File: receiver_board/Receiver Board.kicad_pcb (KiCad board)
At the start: 4 copper layers, 24.8 x 17.5 mm, 12 parts, among them P4 SERIAL, SW1 SW_DPST, U1 LM3671, U2 ESP-01, U3 NeoPixel, U4 SN74LVC1T45

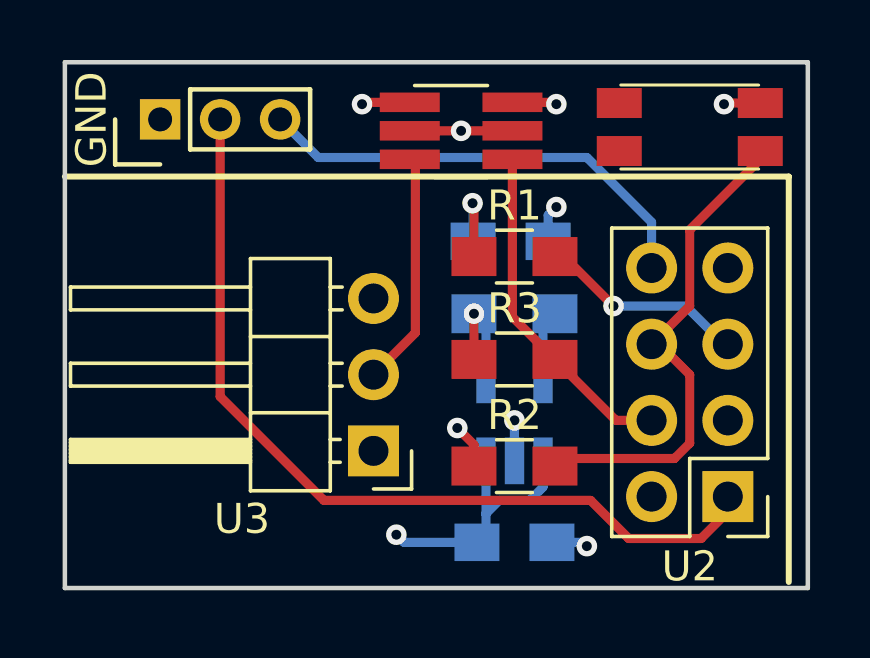
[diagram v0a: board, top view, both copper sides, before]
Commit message: Revised receiver board
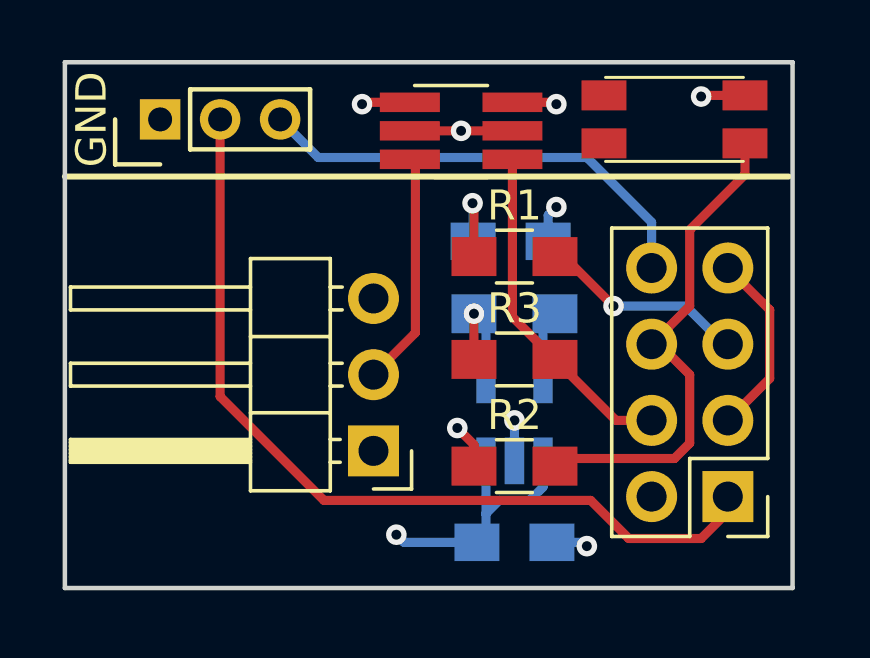
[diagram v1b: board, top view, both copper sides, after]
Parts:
- moved SW1 0.57 mm to (148.0, 132.1)
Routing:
- net VCC: track 9.96 -> 16.2 mm
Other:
- board size 24.8 x 17.5 mm -> 24.3 x 17.5 mm
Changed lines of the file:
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@@
     (links 29)
     (no_connects 0)
-    (area 124.8026 116.600409 152.475001 155.015001)
+    (area 124.8026 116.600409 152.475001 148.082001)
     (thickness 1.6)
-    (drawings 8)
-    (tracks 78)
+    (drawings 7)
+    (tracks 81)
     (zones 0)
     (modules 12)
@@
     (descr "Through hole straight pin header, 2x04, 2.54mm pitch, double rows")
     (tags "Through hole pin header THT 2x04 2.54mm double row")
-    (fp_text reference U2 (at 1.27 -2.33 180) (layer F.SilkS)
+    (fp_text reference U2 (at 1.27 -2.33 180) (layer F.SilkS) hide
       (effects (font (size 1 1) (thickness 0.15)))
     )
@@
     (descr "Through hole angled pin header, 1x03, 2.54mm pitch, 6mm pin length, single row")
     (tags "Through hole angled pin header THT 1x03 2.54mm single row")
-    (fp_text reference U3 (at 4.385 -2.27 180) (layer F.SilkS)
+    (fp_text reference U3 (at 4.385 -2.27 180) (layer F.SilkS) hide
       (effects (font (size 1 1) (thickness 0.15)))
     )
@@
   )
   (module nebrius-switch:KMR641NG (layer F.Cu)
-    (at 148.463 132.334 180)
+    (at 147.955 132.08 180)
     (fp_text reference SW1 (at 0 4 180) (layer F.SilkS) hide
       (effects (font (size 1 1) (thickness 0.15)))
@@
     )
   )
-  (gr_line (start 127.635 130.175) (end 152.4 130.175) (angle 90) (layer Edge.Cuts) (width 0.15))
-  (gr_line (start 127.635 147.701) (end 152.4 147.701) (angle 90) (layer Edge.Cuts) (width 0.15))
+  (gr_line (start 127.635 130.175) (end 151.892 130.175) (angle 90) (layer Edge.Cuts) (width 0.15))
+  (gr_line (start 127.635 147.701) (end 151.892 147.701) (angle 90) (layer Edge.Cuts) (width 0.15))
   (gr_line (start 127.635 130.175) (end 127.635 147.701) (angle 90) (layer Edge.Cuts) (width 0.15))
-  (gr_line (start 152.4 147.701) (end 152.4 130.175) (angle 90) (layer Edge.Cuts) (width 0.15))
+  (gr_line (start 151.892 147.701) (end 151.892 130.175) (angle 90) (layer Edge.Cuts) (width 0.15))
   (gr_text "Raver Lights\nReceiver 3.0\nCopyright\nBryan Hughes" (at 132.08 140.97 90) (layer B.SilkS)
     (effects (font (size 1.016 1.016) (thickness 0.1524)) (justify mirror))
@@
   )
   (gr_line (start 151.765 133.985) (end 127.635 133.985) (angle 90) (layer F.SilkS) (width 0.2))
-  (gr_line (start 151.765 147.5) (end 151.765 133.985) (angle 90) (layer F.SilkS) (width 0.2))
   (segment (start 143.571 140.763) (end 143.571 138.957) (width 0.3048) (layer B.Cu) (net 1))
   (segment (start 143.571 138.957) (end 143.971 138.557) (width 0.3048) (layer B.Cu) (net 1))
@@
   (via (at 137.541 131.572) (size 0.6858) (drill 0.3302) (layers F.Cu B.Cu) (net 2))
   (segment (start 137.602 131.511) (end 137.541 131.572) (width 0.3048) (layer F.Cu) (net 2))
+  (segment (start 150.305 131.28) (end 148.882 131.28) (width 0.3048) (layer F.Cu) (net 3))
+  (via (at 148.844 131.318) (size 0.6858) (drill 0.3302) (layers F.Cu B.Cu) (net 3))
+  (segment (start 148.882 131.28) (end 148.844 131.318) (width 0.3048) (layer F.Cu) (net 3))
   (segment (start 143.744 136.144) (end 143.744 135.275) (width 0.3048) (layer B.Cu) (net 3))
   (via (at 144.018 135.001) (size 0.6858) (drill 0.3302) (layers F.Cu B.Cu) (net 3))
@@
   (segment (start 142.621 143.463) (end 142.621 142.113) (width 0.3048) (layer B.Cu) (net 3))
   (via (at 142.621 142.113) (size 0.6858) (drill 0.3302) (layers F.Cu B.Cu) (net 3))
-  (segment (start 150.813 131.534) (end 149.644 131.534) (width 0.3048) (layer F.Cu) (net 3))
-  (via (at 149.606 131.572) (size 0.6858) (drill 0.3302) (layers F.Cu B.Cu) (net 3))
-  (segment (start 149.644 131.534) (end 149.606 131.572) (width 0.3048) (layer F.Cu) (net 3))
+  (segment (start 149.733 137.033) (end 151.13 138.43) (width 0.3048) (layer F.Cu) (net 4))
+  (segment (start 151.13 140.716) (end 149.733 142.113) (width 0.3048) (layer F.Cu) (net 4))
+  (segment (start 151.13 138.43) (end 151.13 140.716) (width 0.3048) (layer F.Cu) (net 4))
   (segment (start 141.271 143.637) (end 141.271 142.922) (width 0.3048) (layer F.Cu) (net 4))
   (via (at 140.716 142.367) (size 0.6858) (drill 0.3302) (layers F.Cu B.Cu) (net 4))
@@
   (segment (start 145.923 138.303) (end 144.272 136.652) (width 0.3048) (layer F.Cu) (net 7))
   (segment (start 144.272 136.652) (end 143.971 136.652) (width 0.3048) (layer F.Cu) (net 7))
+  (segment (start 150.305 132.88) (end 150.305 133.921) (width 0.3048) (layer F.Cu) (net 8))
+  (segment (start 148.463 138.303) (end 147.193 139.573) (width 0.3048) (layer F.Cu) (net 8))
+  (segment (start 148.463 135.763) (end 148.463 138.303) (width 0.3048) (layer F.Cu) (net 8))
+  (segment (start 150.305 133.921) (end 148.463 135.763) (width 0.3048) (layer F.Cu) (net 8))
   (segment (start 147.193 139.573) (end 147.447 139.573) (width 0.3048) (layer F.Cu) (net 8))
   (segment (start 147.447 139.573) (end 148.463 140.589) (width 0.3048) (layer F.Cu) (net 8))
@@
   (segment (start 148.463 140.589) (end 148.463 142.875) (width 0.3048) (layer F.Cu) (net 8))
   (segment (start 144.225 143.383) (end 143.971 143.637) (width 0.3048) (layer F.Cu) (net 8))
-  (segment (start 150.813 133.134) (end 150.813 133.413) (width 0.3048) (layer F.Cu) (net 8))
-  (segment (start 150.813 133.413) (end 148.463 135.763) (width 0.3048) (layer F.Cu) (net 8))
-  (segment (start 148.463 135.763) (end 148.463 138.303) (width 0.3048) (layer F.Cu) (net 8))
-  (segment (start 148.463 138.303) (end 147.193 139.573) (width 0.3048) (layer F.Cu) (net 8))
   (segment (start 142.553 133.411) (end 142.553 138.663) (width 0.3048) (layer F.Cu) (net 9))
   (segment (start 142.553 138.663) (end 143.971 140.081) (width 0.3048) (layer F.Cu) (net 9))
@@
     (polygon
       (pts
-        (xy 152.4 148.082) (xy 127.635 148.082) (xy 127.635 130.175) (xy 152.4 130.175)
+        (xy 152.4 147.701) (xy 127.635 147.701) (xy 127.635 130.175) (xy 152.4 130.175)
       )
     )
@@
     (polygon
       (pts
-        (xy 139.446 148.082) (xy 127.635 148.082) (xy 127.635 130.175) (xy 139.446 130.175)
+        (xy 139.446 147.701) (xy 127.635 147.701) (xy 127.635 130.175) (xy 139.446 130.175)
       )
     )
@@
     (polygon
       (pts
-        (xy 152.4 148.082) (xy 140.081 148.082) (xy 140.081 130.175) (xy 152.4 130.175)
+        (xy 151.892 147.701) (xy 140.081 147.701) (xy 140.081 130.175) (xy 151.892 130.175)
       )
     )

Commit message: Added copyright date
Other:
- board text added: "Raver Lights Receiver 3.0 Copyright 2018 Bryan Hughes"
- board text removed: "Raver Lights Receiver 3.0 Copyright Bryan Hughes"
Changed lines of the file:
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@@
   (gr_line (start 127.635 130.175) (end 127.635 147.701) (angle 90) (layer Edge.Cuts) (width 0.15))
   (gr_line (start 151.892 147.701) (end 151.892 130.175) (angle 90) (layer Edge.Cuts) (width 0.15))
-  (gr_text "Raver Lights\nReceiver 3.0\nCopyright\nBryan Hughes" (at 132.08 140.97 90) (layer B.SilkS)
+  (gr_text "Raver Lights\nReceiver 3.0\nCopyright 2018\nBryan Hughes" (at 132.08 140.97 90) (layer B.SilkS)
     (effects (font (size 1.016 1.016) (thickness 0.1524)) (justify mirror))
   )

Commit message: Added BOM and fuse
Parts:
- added F1: Fuse, Resistors_SMD:R_0805_HandSoldering, F.Cu at (140.0, 146.2)
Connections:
- C1 pad 1: +5V -> Net-(C1-Pad1)
- U1 pad 1: +5V -> Net-(C1-Pad1)
- U1 pad 3: +5V -> Net-(C1-Pad1)
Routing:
- net +5V: track 10.4 -> 3.09 mm
- net Net-(C1-Pad1): track 0.00 -> 6.12 mm, vias 0 -> 1
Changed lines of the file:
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@@
 (kicad_pcb (version 4) (host pcbnew 4.0.7)
   (general
-    (links 29)
+    (links 30)
     (no_connects 0)
-    (area 124.8026 116.600409 152.475001 148.082001)
+    (area 127.559999 130.099999 151.967001 147.776001)
     (thickness 1.6)
     (drawings 7)
-    (tracks 81)
+    (tracks 83)
     (zones 0)
-    (modules 12)
-    (nets 11)
+    (modules 13)
+    (nets 12)
   )
   (page A4)
@@
   (net 9 "Net-(R3-Pad2)")
   (net 10 "Net-(U3-Pad2)")
+  (net 11 "Net-(C1-Pad1)")
   (net_class Default "This is the default net class."
     (clearance 0.1524)
@@
     (add_net +5V)
     (add_net GND)
+    (add_net "Net-(C1-Pad1)")
     (add_net "Net-(L1-Pad1)")
     (add_net "Net-(P4-Pad2)")
@@
     (fp_line (start -0.5 -0.85) (end 0.5 -0.85) (layer B.SilkS) (width 0.15))
     (pad 1 smd rect (at -1.25 0) (size 1.5 1.25) (layers B.Cu B.Paste B.Mask)
-      (net 2 +5V))
+      (net 11 "Net-(C1-Pad1)"))
     (pad 2 smd rect (at 1.25 0) (size 1.5 1.25) (layers B.Cu B.Paste B.Mask)
       (net 3 GND))
@@
     (fp_line (start 2.38 -1.8) (end -2.38 -1.8) (layer B.CrtYd) (width 0.05))
     (pad 1 smd rect (at -1.35 0.95 90) (size 1.56 0.65) (layers B.Cu B.Paste B.Mask)
-      (net 2 +5V))
+      (net 11 "Net-(C1-Pad1)"))
     (pad 2 smd rect (at -1.35 0 90) (size 1.56 0.65) (layers B.Cu B.Paste B.Mask)
       (net 3 GND))
     (pad 3 smd rect (at -1.35 -0.95 90) (size 1.56 0.65) (layers B.Cu B.Paste B.Mask)
-      (net 2 +5V))
+      (net 11 "Net-(C1-Pad1)"))
     (pad 4 smd rect (at 1.35 -0.95 90) (size 1.56 0.65) (layers B.Cu B.Paste B.Mask)
       (net 4 VCC))
@@
       (net 1 "Net-(L1-Pad1)"))
     (model ${KISYS3DMOD}/TO_SOT_Packages_SMD.3dshapes\SOT-23-5.wrl
+      (at (xyz 0 0 0))
+      (scale (xyz 1 1 1))
+      (rotate (xyz 0 0 0))
+    )
+  )
+  (module Resistors_SMD:R_0805_HandSoldering (layer F.Cu)
+    (at 139.954 146.177 180)
+    (descr "Resistor SMD 0805, hand soldering")
+    (tags "resistor 0805")
+    (attr smd)
+    (fp_text reference F1 (at 3.302 0 180) (layer F.SilkS)
+      (effects (font (size 1 1) (thickness 0.15)))
+    )
+    (fp_text value Fuse (at 0 1.75 180) (layer F.Fab) hide
+      (effects (font (size 1 1) (thickness 0.15)))
+    )
+    (fp_text user %R (at 0 0 180) (layer F.Fab)
+      (effects (font (size 0.5 0.5) (thickness 0.075)))
+    )
+    (fp_line (start -1 0.62) (end -1 -0.62) (layer F.Fab) (width 0.1))
+    (fp_line (start 1 0.62) (end -1 0.62) (layer F.Fab) (width 0.1))
+    (fp_line (start 1 -0.62) (end 1 0.62) (layer F.Fab) (width 0.1))
+    (fp_line (start -1 -0.62) (end 1 -0.62) (layer F.Fab) (width 0.1))
+    (fp_line (start 0.6 0.88) (end -0.6 0.88) (layer F.SilkS) (width 0.12))
+    (fp_line (start -0.6 -0.88) (end 0.6 -0.88) (layer F.SilkS) (width 0.12))
+    (fp_line (start -2.35 -0.9) (end 2.35 -0.9) (layer F.CrtYd) (width 0.05))
+    (fp_line (start -2.35 -0.9) (end -2.35 0.9) (layer F.CrtYd) (width 0.05))
+    (fp_line (start 2.35 0.9) (end 2.35 -0.9) (layer F.CrtYd) (width 0.05))
+    (fp_line (start 2.35 0.9) (end -2.35 0.9) (layer F.CrtYd) (width 0.05))
+    (pad 1 smd rect (at -1.35 0 180) (size 1.5 1.3) (layers F.Cu F.Paste F.Mask)
+      (net 11 "Net-(C1-Pad1)"))
+    (pad 2 smd rect (at 1.35 0 180) (size 1.5 1.3) (layers F.Cu F.Paste F.Mask)
+      (net 2 +5V))
+    (model ${KISYS3DMOD}/Resistors_SMD.3dshapes/R_0805.wrl
       (at (xyz 0 0 0))
       (scale (xyz 1 1 1))
@@
   (segment (start 143.571 140.763) (end 143.571 138.957) (width 0.3048) (layer B.Cu) (net 1))
   (segment (start 143.571 138.957) (end 143.971 138.557) (width 0.3048) (layer B.Cu) (net 1))
-  (segment (start 143.571 143.463) (end 143.571 144.338) (width 0.3048) (layer B.Cu) (net 2))
-  (segment (start 142.113 144.78) (end 141.671 145.222) (width 0.3048) (layer B.Cu) (net 2))
-  (segment (start 143.129 144.78) (end 142.113 144.78) (width 0.3048) (layer B.Cu) (net 2))
-  (segment (start 143.571 144.338) (end 143.129 144.78) (width 0.3048) (layer B.Cu) (net 2))
-  (segment (start 141.671 143.463) (end 141.671 145.222) (width 0.3048) (layer B.Cu) (net 2))
-  (segment (start 141.671 145.222) (end 141.671 145.877) (width 0.3048) (layer B.Cu) (net 2))
-  (segment (start 141.671 145.877) (end 141.371 146.177) (width 0.3048) (layer B.Cu) (net 2))
-  (segment (start 141.371 146.177) (end 138.938 146.177) (width 0.3048) (layer B.Cu) (net 2))
-  (via (at 138.684 145.923) (size 0.6858) (drill 0.3302) (layers F.Cu B.Cu) (net 2))
-  (segment (start 138.938 146.177) (end 138.684 145.923) (width 0.3048) (layer B.Cu) (net 2))
+  (segment (start 138.604 146.177) (end 137.668 146.177) (width 0.3048) (layer F.Cu) (net 2))
+  (via (at 137.287 145.796) (size 0.6858) (drill 0.3302) (layers F.Cu B.Cu) (net 2))
+  (segment (start 137.668 146.177) (end 137.287 145.796) (width 0.3048) (layer F.Cu) (net 2))
   (segment (start 139.133 131.511) (end 137.602 131.511) (width 0.3048) (layer F.Cu) (net 2))
   (via (at 137.541 131.572) (size 0.6858) (drill 0.3302) (layers F.Cu B.Cu) (net 2))
@@
   (segment (start 139.319 139.192) (end 139.319 133.597) (width 0.3048) (layer F.Cu) (net 10))
   (segment (start 139.319 133.597) (end 139.133 133.411) (width 0.3048) (layer F.Cu) (net 10))
+  (segment (start 143.571 143.463) (end 143.571 144.465) (width 0.3048) (layer B.Cu) (net 11))
+  (segment (start 142.113 144.78) (end 141.671 145.222) (width 0.3048) (layer B.Cu) (net 11))
+  (segment (start 143.256 144.78) (end 142.113 144.78) (width 0.3048) (layer B.Cu) (net 11))
+  (segment (start 143.571 144.465) (end 143.256 144.78) (width 0.3048) (layer B.Cu) (net 11))
+  (via (at 141.304 146.177) (size 0.6858) (drill 0.3302) (layers F.Cu B.Cu) (net 11))
+  (segment (start 141.304 146.177) (end 141.371 146.177) (width 0.3048) (layer B.Cu) (net 11))
+  (segment (start 141.671 145.222) (end 141.671 145.877) (width 0.3048) (layer B.Cu) (net 11))
+  (segment (start 141.671 145.877) (end 141.371 146.177) (width 0.3048) (layer B.Cu) (net 11))
+  (segment (start 141.671 143.463) (end 141.671 145.222) (width 0.3048) (layer B.Cu) (net 11))
   (zone (net 3) (net_name GND) (layer Ground.Plane) (hatch edge 0.508)
     (connect_pads (clearance 0.508))
